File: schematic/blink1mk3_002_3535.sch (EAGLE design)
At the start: 15 parts, among them U1 EFM32HG309F64G, X2 USBPCB2

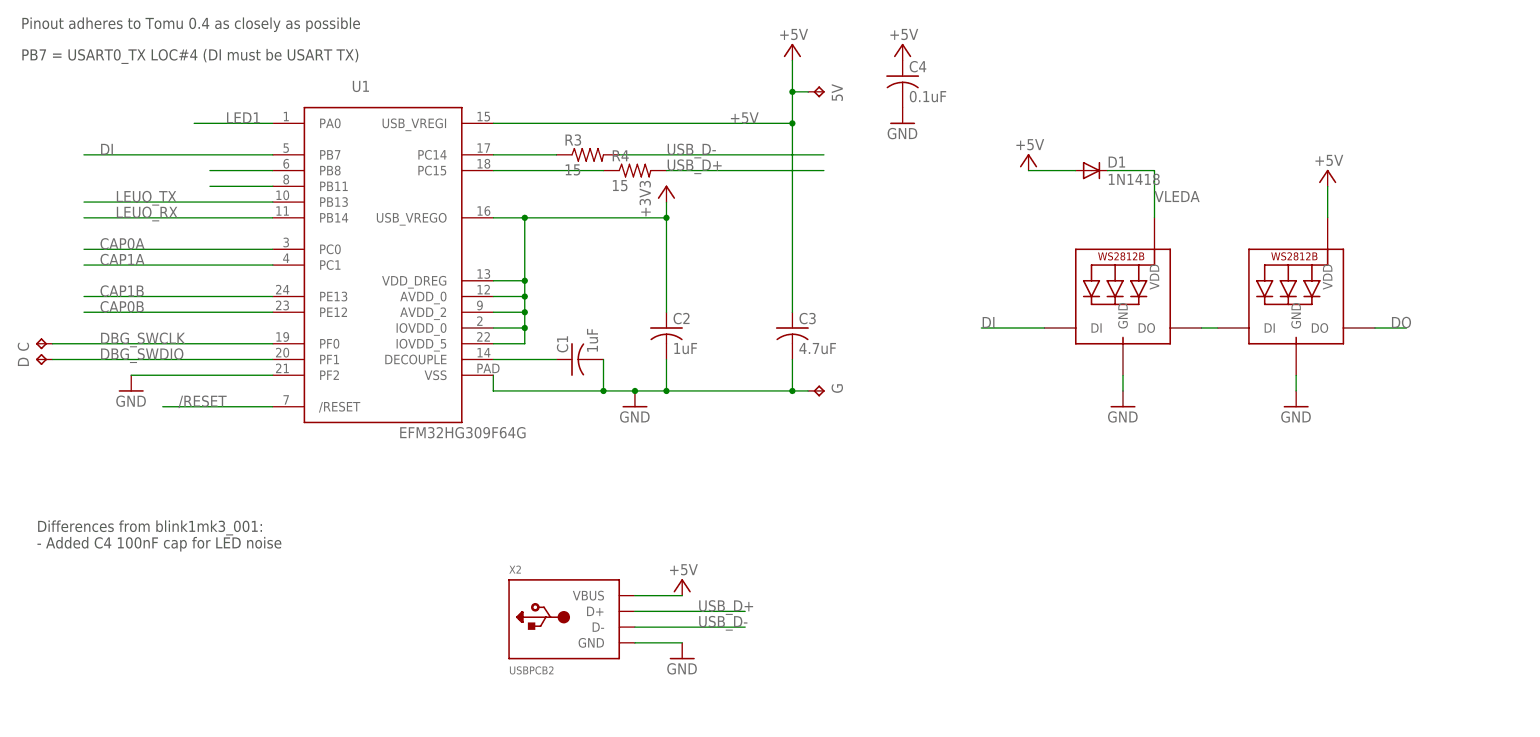
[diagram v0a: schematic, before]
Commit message: added business card variant, and 3535 LED variant
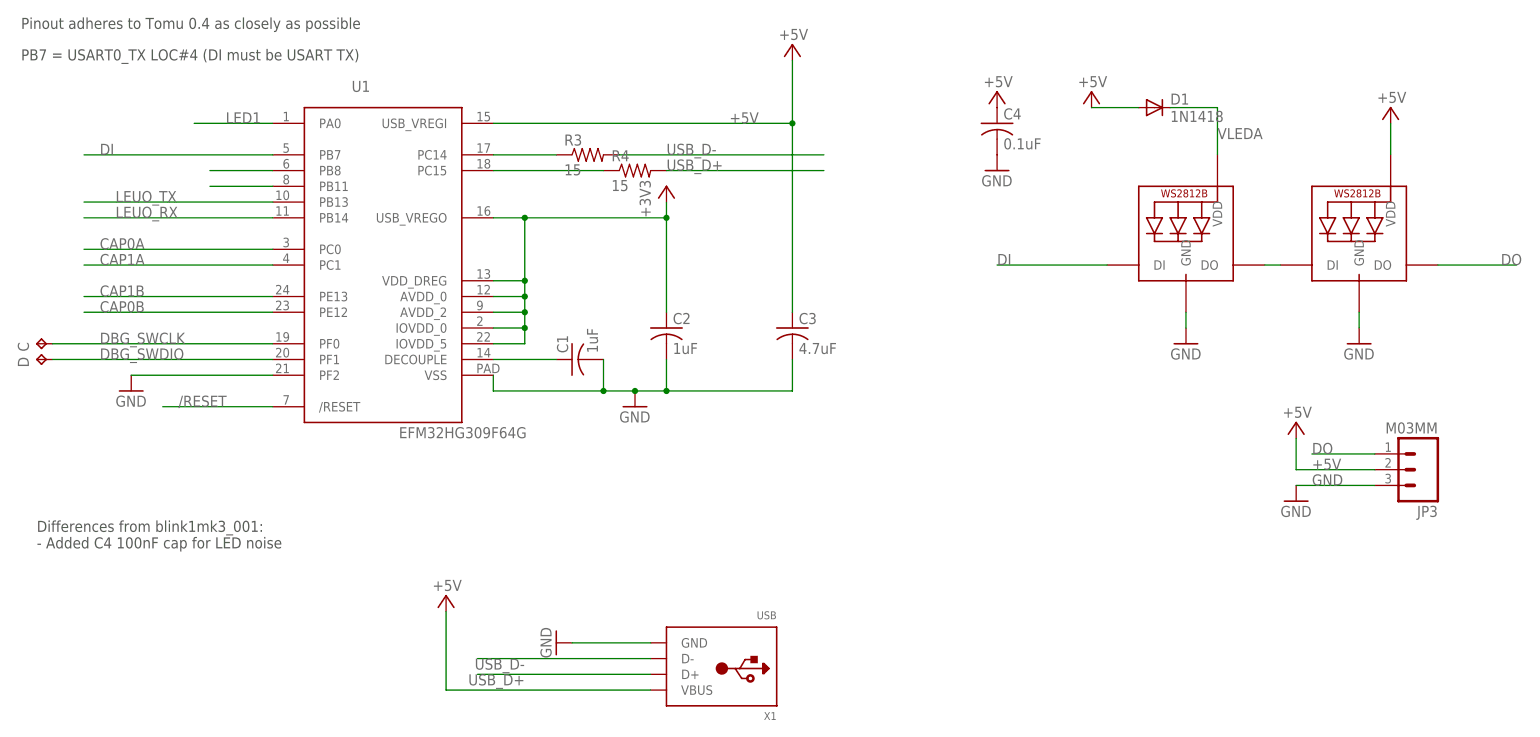
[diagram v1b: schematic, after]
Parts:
- removed 5V, G: TPTP10R, testpad:TPTP10R
- removed X2: USBPCB2, todstuff:USBPCB2
- added JP3: M03MM, todstuff:M03MM
- added X1: USB, todstuff:USB
- LED1, LED2: value WS2812B4020SIDE -> WS2812B3535; device todstuff:WS2812B4020SIDE -> adafruit:WS2812B3535
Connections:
- net +5V: now also JP3.2, X1.VBUS; no longer 5V.TP, X2.VBUS
- net DO: now also JP3.1
- net GND: now also JP3.3, X1.GND; no longer G.TP, X2.GND
- net USB_D+: now also X1.D+; no longer X2.D+
- net USB_D-: now also X1.D-; no longer X2.D-
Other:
- moved on the sheet: C4, D1
